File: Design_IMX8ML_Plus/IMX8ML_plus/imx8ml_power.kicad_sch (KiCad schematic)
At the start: 33 parts

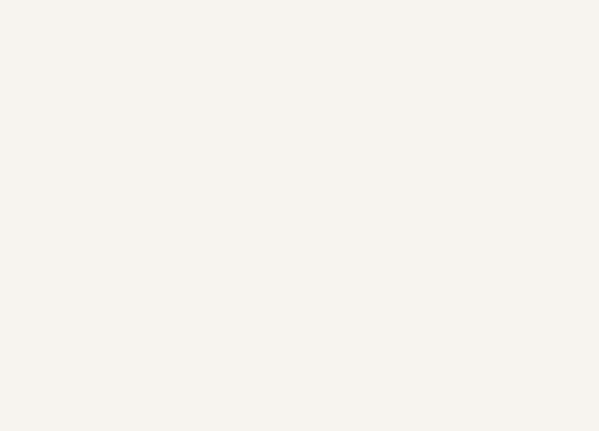
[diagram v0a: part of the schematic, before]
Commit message: Add resistors to PMIC
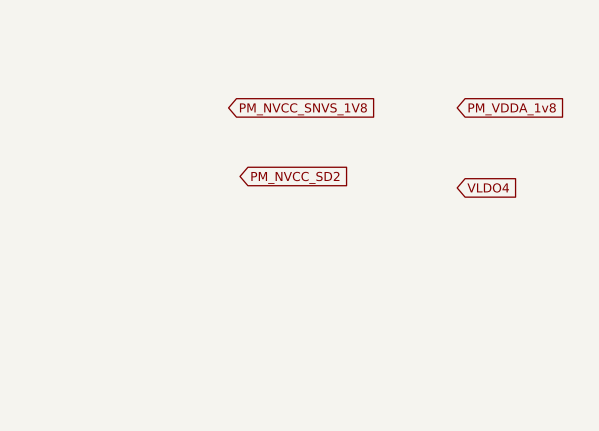
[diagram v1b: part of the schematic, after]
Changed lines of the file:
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@@
     (effects (font (size 1.27 1.27)) (justify left bottom))
+  )
+  (global_label "PM_VDDA_1v8" (shape input) (at 260.35 29.21 0) (fields_autoplaced)
+    (effects (font (size 1 1)) (justify left))
+    (property "Intersheetrefs" "${INTERSHEET_REFS}" (at 272.6855 29.21 0)
+      (effects (font (size 1.27 1.27)) (justify left) hide)
+    )
   )
   (global_label "PM_NVCC_DRAM_1V1" (shape input) (at 34.29 80.01 180) (fields_autoplaced)
@@
     )
   )
+  (global_label "PM_NVCC_SD2" (shape input) (at 236.22 36.83 0) (fields_autoplaced)
+    (effects (font (size 1 1)) (justify left))
+    (property "Intersheetrefs" "${INTERSHEET_REFS}" (at 248.9841 36.83 0)
+      (effects (font (size 1.27 1.27)) (justify left) hide)
+    )
+  )
+  (global_label "PM_NVCC_SNVS_1V8" (shape input) (at 234.95 29.21 0) (fields_autoplaced)
+    (effects (font (size 1 1)) (justify left))
+    (property "Intersheetrefs" "${INTERSHEET_REFS}" (at 252.1426 29.21 0)
+      (effects (font (size 1.27 1.27)) (justify left) hide)
+    )
+  )
+  (global_label "VLDO4" (shape input) (at 260.35 38.1 0) (fields_autoplaced)
+    (effects (font (size 1 1)) (justify left))
+    (property "Intersheetrefs" "${INTERSHEET_REFS}" (at 267.3045 38.1 0)
+      (effects (font (size 1.27 1.27)) (justify left) hide)
+    )
+  )

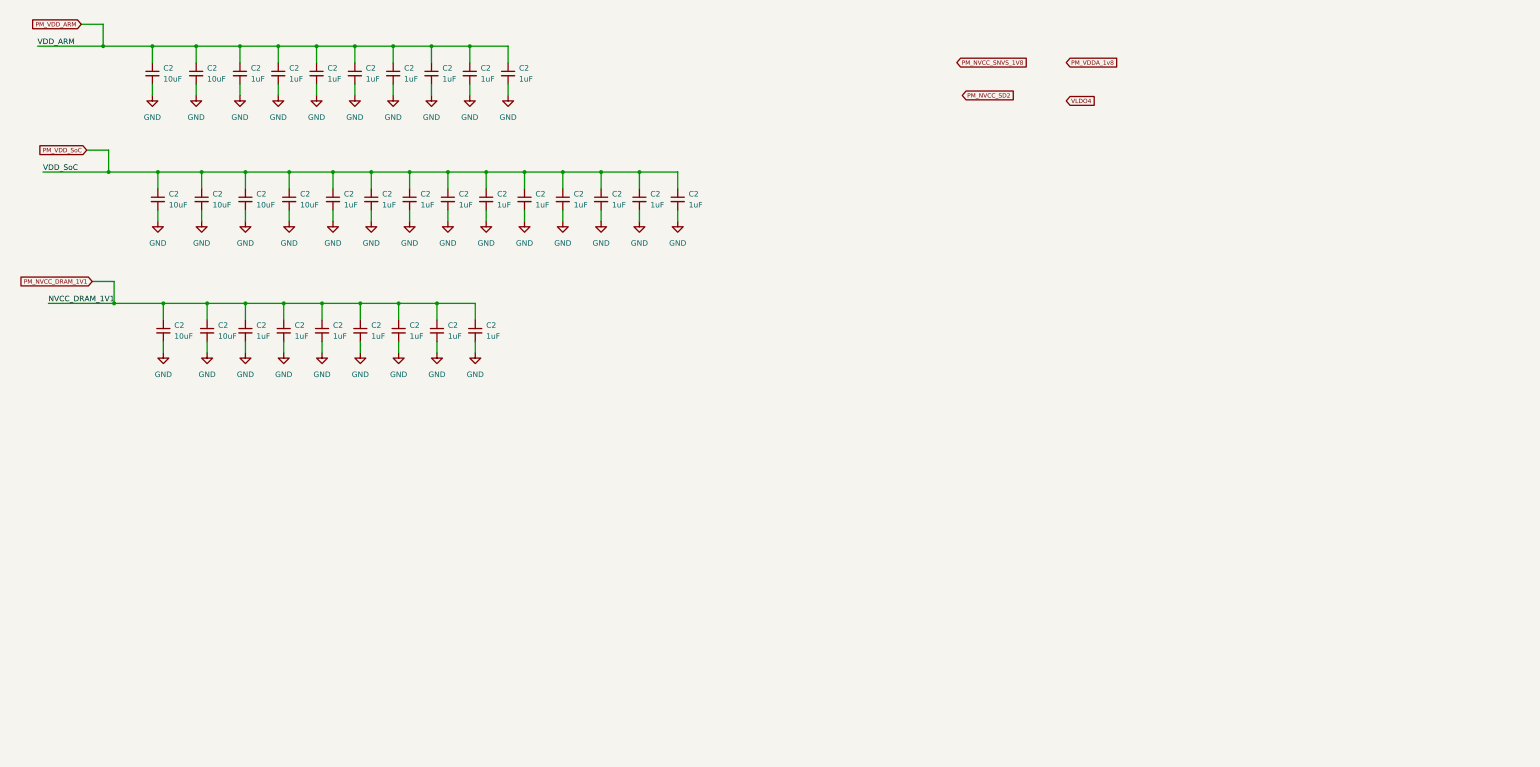
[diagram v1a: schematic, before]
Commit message: Add interface io pins
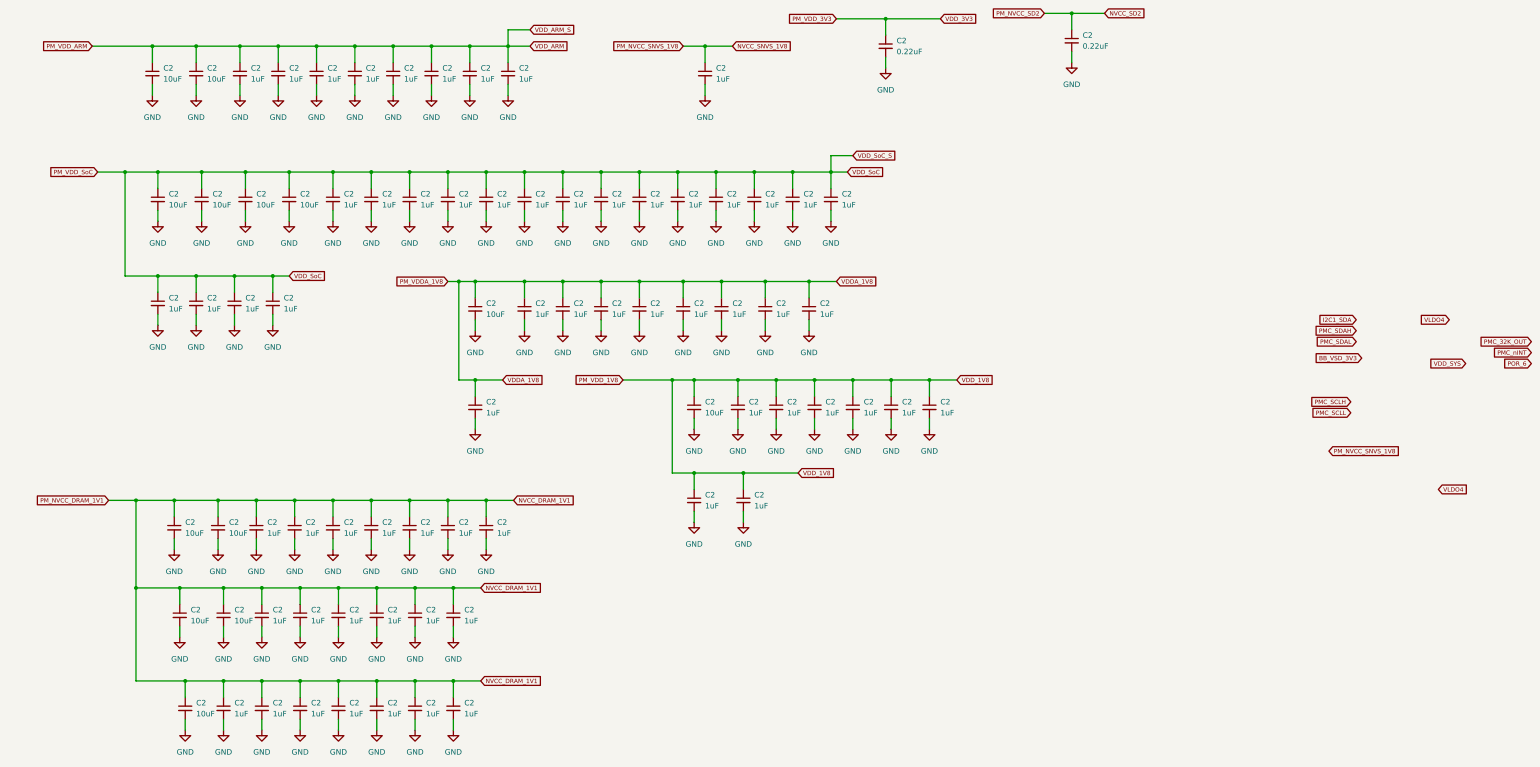
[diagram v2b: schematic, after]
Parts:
- added C2 (x39): 1uF, Capacitor_SMD:C_0201_0603Metric_Pad0.64x0.40mm_HandSolder, symbol Device:C_Small
- added C2 (x5): 10uF, Capacitor_SMD:C_0402_1005Metric, symbol Device:C_Small
- added C2 (x2): 0.22uF, Capacitor_SMD:C_0201_0603Metric_Pad0.64x0.40mm_HandSolder, symbol Device:C_Small
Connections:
- net GND: now also C2.2, C2.2, C2.2, C2.2, C2.2, C2.2, C2.2, C2.2, C2.2, C2.2, C2.2, C2.2, C2.2, C2.2, C2.2, C2.2, C2.2, C2.2, C2.2, C2.2, C2.2, C2.2, C2.2, C2.2, C2.2, C2.2, C2.2, C2.2, C2.2, C2.2, C2.2, C2.2, C2.2, C2.2, C2.2, C2.2, C2.2, C2.2, C2.2, C2.2, C2.2, C2.2, C2.2, C2.2, C2.2, C2.2
- net PM_VDD_SoC: now also C2.1, C2.1, C2.1, C2.1, C2.1, C2.1, C2.1, C2.1
- net PM_NVCC_DRAM_1V1 renamed NVCC_DRAM_1V1
- net NVCC_DRAM_1V1: now also C2.1, C2.1, C2.1, C2.1, C2.1, C2.1, C2.1, C2.1, C2.1, C2.1, C2.1, C2.1, C2.1, C2.1, C2.1, C2.1
- new net NVCC_SD2: C2.1
- new net NVCC_SNVS_1V8: C2.1
- new net PM_VDDA_1V8: C2.1, C2.1, C2.1, C2.1, C2.1, C2.1, C2.1, C2.1, C2.1, C2.1
- new net PM_VDD_1V8: C2.1, C2.1, C2.1, C2.1, C2.1, C2.1, C2.1, C2.1, C2.1
- new net PM_VDD_3V3: C2.1
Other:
- moved on the sheet: C2

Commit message: processor capacitors location
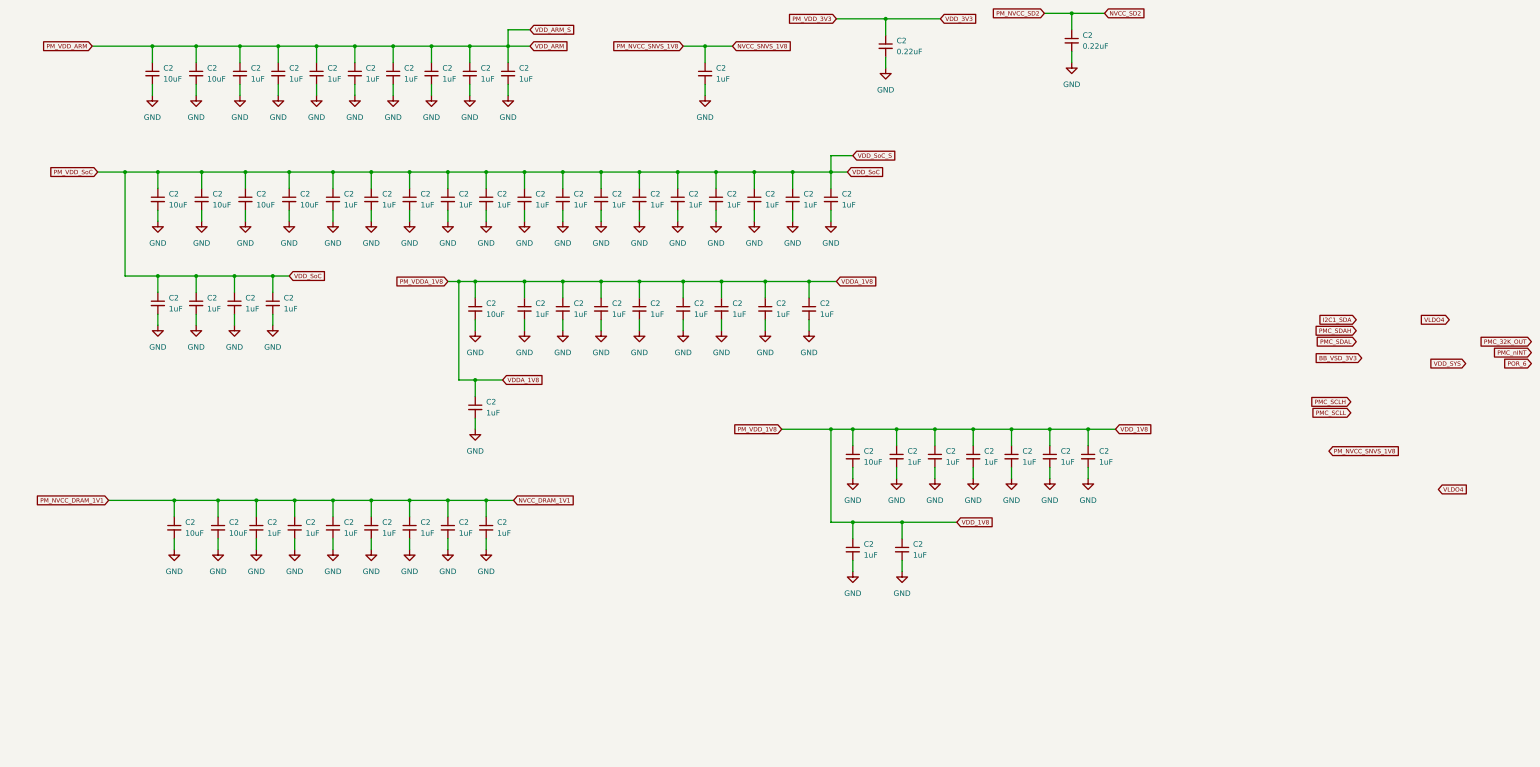
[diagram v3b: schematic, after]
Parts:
- removed C2 (x13): 1uF, Capacitor_SMD:C_0201_0603Metric_Pad0.64x0.40mm_HandSolder, symbol Device:C_Small
- removed C2 (x3): 10uF, Capacitor_SMD:C_0402_1005Metric, symbol Device:C_Small
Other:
- moved on the sheet: C2

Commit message: Add SPB228 WIFI/BLE module
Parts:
- renumbered C2 to C100, C2 to C101, C2 to C102, C2 to C103, C2 to C104, C2 to C105, C2 to C106, C2 to C107, C2 to C108, C2 to C109, C2 to C110, C2 to C111, C2 to C112, C2 to C113, C2 to C114, C2 to C115, C2 to C116, C2 to C117, C2 to C118, C2 to C119, C2 to C120, C2 to C121, C2 to C122, C2 to C123, C2 to C132, C2 to C141, C2 to C25, C2 to C26, C2 to C27, C2 to C28, C2 to C29, C2 to C30, C2 to C31, C2 to C32, C2 to C33, C2 to C34, C2 to C35, C2 to C36, C2 to C37, C2 to C38, C2 to C39, C2 to C40, C2 to C41, C2 to C42, C2 to C43, C2 to C44, C2 to C45, C2 to C46, C2 to C47, C2 to C48, C2 to C49, C2 to C50, C2 to C56, C2 to C57, C2 to C58, C2 to C59, C2 to C60, C2 to C61, C2 to C62, C2 to C96, C2 to C97, C2 to C98, C2 to C99

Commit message: reorganization of the componentes
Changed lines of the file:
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@@
 	(global_label "BB_VSD_3V3"
 		(shape input)
-		(at 328.93 97.79 180)
-		(fields_autoplaced yes)
-		(effects
-			(font
-				(size 1 1)
-			)
-			(justify right)
-		)
-		(property "Intersheetrefs" "${INTERSHEET_REFS}"
-			(at 317.5469 97.79 0)
+		(at 242.57 62.23 180)
+		(fields_autoplaced yes)
+		(effects
+			(font
+				(size 1 1)
+			)
+			(justify right)
+		)
+		(property "Intersheetrefs" "${INTERSHEET_REFS}"
+			(at 231.1869 62.23 0)
 			(effects
 				(font
@@
 	(global_label "I2C1_SDA"
 		(shape input)
-		(at 327.66 88.9 180)
-		(fields_autoplaced yes)
-		(effects
-			(font
-				(size 1 1)
-			)
-			(justify right)
-		)
-		(property "Intersheetrefs" "${INTERSHEET_REFS}"
-			(at 318.4197 88.9 0)
+		(at 241.3 53.34 180)
+		(fields_autoplaced yes)
+		(effects
+			(font
+				(size 1 1)
+			)
+			(justify right)
+		)
+		(property "Intersheetrefs" "${INTERSHEET_REFS}"
+			(at 232.0597 53.34 0)
 			(effects
 				(font
@@
 	(global_label "VLDO4"
 		(shape input)
-		(at 349.25 88.9 180)
-		(fields_autoplaced yes)
-		(effects
-			(font
-				(size 1 1)
-			)
-			(justify right)
-		)
-		(property "Intersheetrefs" "${INTERSHEET_REFS}"
-			(at 342.2955 88.9 0)
+		(at 262.89 53.34 180)
+		(fields_autoplaced yes)
+		(effects
+			(font
+				(size 1 1)
+			)
+			(justify right)
+		)
+		(property "Intersheetrefs" "${INTERSHEET_REFS}"
+			(at 255.9355 53.34 0)
 			(effects
 				(font
@@
 	(global_label "PMC_SCLH"
 		(shape input)
-		(at 326.39 107.95 180)
-		(fields_autoplaced yes)
-		(effects
-			(font
-				(size 1 1)
-			)
-			(justify right)
-		)
-		(property "Intersheetrefs" "${INTERSHEET_REFS}"
-			(at 316.3878 107.95 0)
+		(at 240.03 72.39 180)
+		(fields_autoplaced yes)
+		(effects
+			(font
+				(size 1 1)
+			)
+			(justify right)
+		)
+		(property "Intersheetrefs" "${INTERSHEET_REFS}"
+			(at 230.0278 72.39 0)
 			(effects
 				(font
@@
 	(global_label "PMC_SCLL"
 		(shape input)
-		(at 326.39 110.49 180)
-		(fields_autoplaced yes)
-		(effects
-			(font
-				(size 1 1)
-			)
-			(justify right)
-		)
-		(property "Intersheetrefs" "${INTERSHEET_REFS}"
-			(at 316.6259 110.49 0)
+		(at 240.03 74.93 180)
+		(fields_autoplaced yes)
+		(effects
+			(font
+				(size 1 1)
+			)
+			(justify right)
+		)
+		(property "Intersheetrefs" "${INTERSHEET_REFS}"
+			(at 230.2659 74.93 0)
 			(effects
 				(font
@@
 	(global_label "PMC_SDAH"
 		(shape input)
-		(at 327.66 91.44 180)
-		(fields_autoplaced yes)
-		(effects
-			(font
-				(size 1 1)
-			)
-			(justify right)
-		)
-		(property "Intersheetrefs" "${INTERSHEET_REFS}"
-			(at 317.6102 91.44 0)
+		(at 241.3 55.88 180)
+		(fields_autoplaced yes)
+		(effects
+			(font
+				(size 1 1)
+			)
+			(justify right)
+		)
+		(property "Intersheetrefs" "${INTERSHEET_REFS}"
+			(at 231.2502 55.88 0)
 			(effects
 				(font
@@
 	(global_label "POR_6"
 		(shape input)
-		(at 368.3 99.06 180)
-		(fields_autoplaced yes)
-		(effects
-			(font
-				(size 1 1)
-			)
-			(justify right)
-		)
-		(property "Intersheetrefs" "${INTERSHEET_REFS}"
-			(at 361.2502 99.06 0)
+		(at 281.94 63.5 180)
+		(fields_autoplaced yes)
+		(effects
+			(font
+				(size 1 1)
+			)
+			(justify right)
+		)
+		(property "Intersheetrefs" "${INTERSHEET_REFS}"
+			(at 274.8902 63.5 0)
 			(effects
 				(font
@@
 	(global_label "PMC_32K_OUT"
 		(shape input)
-		(at 368.3 93.98 180)
-		(fields_autoplaced yes)
-		(effects
-			(font
-				(size 1 1)
-			)
-			(justify right)
-		)
-		(property "Intersheetrefs" "${INTERSHEET_REFS}"
-			(at 355.5835 93.98 0)
+		(at 281.94 58.42 180)
+		(fields_autoplaced yes)
+		(effects
+			(font
+				(size 1 1)
+			)
+			(justify right)
+		)
+		(property "Intersheetrefs" "${INTERSHEET_REFS}"
+			(at 269.2235 58.42 0)
 			(effects
 				(font
@@
 	(global_label "PMC_SDAL"
 		(shape input)
-		(at 327.66 93.98 180)
-		(fields_autoplaced yes)
-		(effects
-			(font
-				(size 1 1)
-			)
-			(justify right)
-		)
-		(property "Intersheetrefs" "${INTERSHEET_REFS}"
-			(at 317.8483 93.98 0)
+		(at 241.3 58.42 180)
+		(fields_autoplaced yes)
+		(effects
+			(font
+				(size 1 1)
+			)
+			(justify right)
+		)
+		(property "Intersheetrefs" "${INTERSHEET_REFS}"
+			(at 231.4883 58.42 0)
 			(effects
 				(font
@@
 	(global_label "PMC_nINT"
 		(shape input)
-		(at 368.3 96.52 180)
-		(fields_autoplaced yes)
-		(effects
-			(font
-				(size 1 1)
-			)
-			(justify right)
-		)
-		(property "Intersheetrefs" "${INTERSHEET_REFS}"
-			(at 358.9168 96.52 0)
+		(at 281.94 60.96 180)
+		(fields_autoplaced yes)
+		(effects
+			(font
+				(size 1 1)
+			)
+			(justify right)
+		)
+		(property "Intersheetrefs" "${INTERSHEET_REFS}"
+			(at 272.5568 60.96 0)
 			(effects
 				(font
@@
 	(global_label "PM_NVCC_SNVS_1V8"
 		(shape input)
-		(at 321.31 119.38 0)
-		(fields_autoplaced yes)
-		(effects
-			(font
-				(size 1 1)
-			)
-			(justify left)
-		)
-		(property "Intersheetrefs" "${INTERSHEET_REFS}"
-			(at 338.5026 119.38 0)
+		(at 234.95 83.82 0)
+		(fields_autoplaced yes)
+		(effects
+			(font
+				(size 1 1)
+			)
+			(justify left)
+		)
+		(property "Intersheetrefs" "${INTERSHEET_REFS}"
+			(at 252.1426 83.82 0)
 			(effects
 				(font
@@
 	(global_label "VDD_SYS"
 		(shape input)
-		(at 353.06 99.06 180)
-		(fields_autoplaced yes)
-		(effects
-			(font
-				(size 1 1)
-			)
-			(justify right)
-		)
-		(property "Intersheetrefs" "${INTERSHEET_REFS}"
-			(at 344.3912 99.06 0)
+		(at 266.7 63.5 180)
+		(fields_autoplaced yes)
+		(effects
+			(font
+				(size 1 1)
+			)
+			(justify right)
+		)
+		(property "Intersheetrefs" "${INTERSHEET_REFS}"
+			(at 258.0312 63.5 0)
 			(effects
 				(font
@@
 	(global_label "VLDO4"
 		(shape input)
-		(at 346.71 128.27 0)
-		(fields_autoplaced yes)
-		(effects
-			(font
-				(size 1 1)
-			)
-			(justify left)
-		)
-		(property "Intersheetrefs" "${INTERSHEET_REFS}"
-			(at 353.6645 128.27 0)
-			(effects
-				(font
+		(at 260.35 92.71 0)
+		(fields_autoplaced yes)
+		(effects
+			(font
+				(size 1 1)
+			)
+			(justify left)
+		)
+		(property "Intersheetrefs" "${INTERSHEET_REFS}"
+			(at 267.3045 92.71 0)
+			(effects
+				(font

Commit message: [PROCESSOR] Create zones It added power zones in the four layer
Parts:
- renumbered C112 to C100, C99 to C101, C113 to C102, C100 to C103, C116 to C104, C123 to C105, C132 to C106, C117 to C107, C115 to C108, C118 to C109, C119 to C110, C120 to C111, C121 to C112, C141 to C113, C122 to C114, C25 to C52, C35 to C53, C101 to C54, C49 to C55, C26 to C56, C102 to C57, C36 to C58, C50 to C59, C103 to C60, C27 to C61, C45 to C62, C56 to C63, C104 to C64, C28 to C65, C46 to C66, C57 to C67, C29 to C68, C37 to C69, C58 to C70, C30 to C71, C38 to C72, C59 to C73, C31 to C74, C39 to C75, C60 to C76, C32 to C77, C40 to C78, C61 to C79, C33 to C80, C111 to C81, C114 to C82, C41 to C83, C62 to C84, C34 to C85, C42 to C86, C105 to C87, C43 to C88, C106 to C89, C44 to C90, C107 to C91, C47 to C92, C108 to C93, C48 to C94, C109 to C95, C110 to C98, C98 to C99

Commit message: [BB_IMX8MLP IMX8MLP] Actuallizated to 9.0 kicad version
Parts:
- C100, C101, C102, C103, C105, C107, C108, C109, C110, C111, C112, C114, C54, C57, C60, C61, C63, C64, C65, C67, C68, C69, C70, C71, C72, C73, C74, C75, C76, C77, C78, C79, C80, C82, C83, C84, C85, C86, C87, C88, C89, C90, C91, C92, C93, C94, C95, C96, C97, C98, C99: footprint Capacitor_SMD:C_0201_0603Metric_Pad0.64x0.40mm_HandSolder -> Capacitor_SMD:C_0201_0603Metric; MP (none) -> 02016D105MAT2A; Price (none) -> 0.1
- C104, C52, C53, C55, C56, C58, C59, C62, C66, C81: MP (none) -> CL05A106MQ5NUNC; Price (none) -> 0.1
- C106, C113: footprint Capacitor_SMD:C_0201_0603Metric_Pad0.64x0.40mm_HandSolder -> Capacitor_SMD:C_0201_0603Metric; MP (none) -> LMK063BJ224MP-F; Price (none) -> 0.11

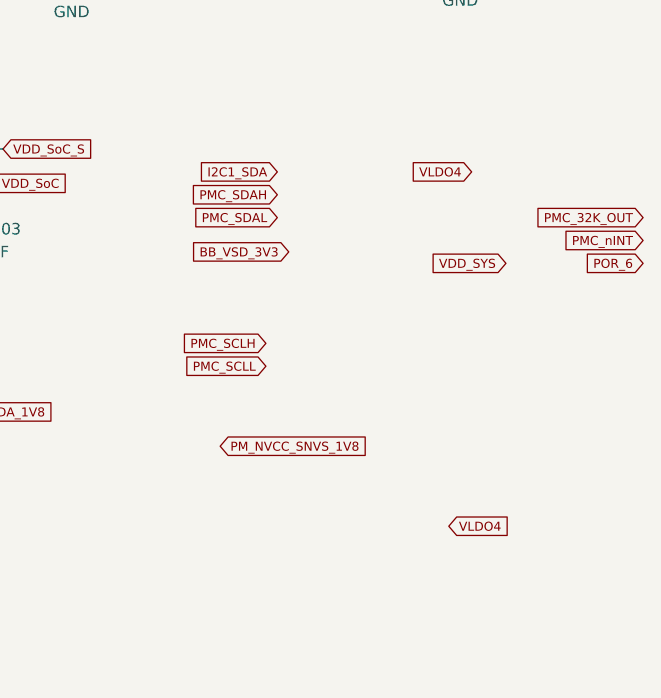
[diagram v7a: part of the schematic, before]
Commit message: [IMX8ML] Add new layer
A new layers was add in the cpu schematic, now it had 8 layer.
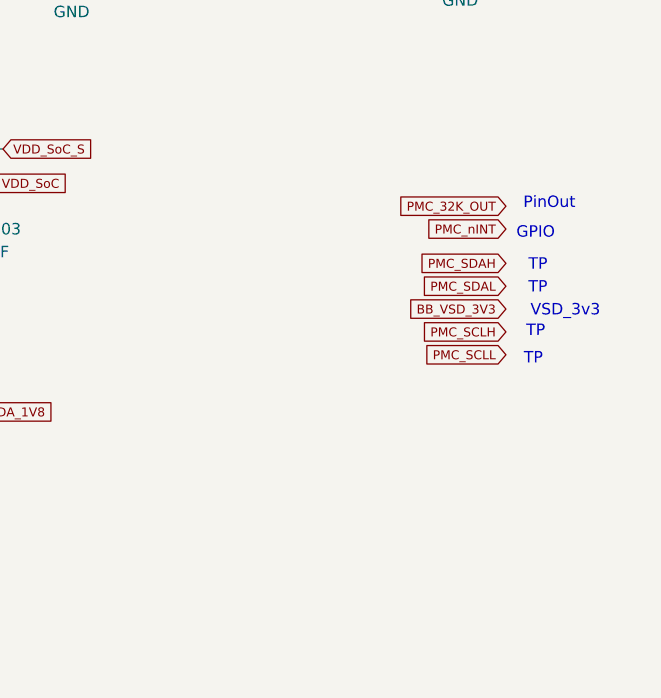
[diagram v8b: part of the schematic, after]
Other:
- note added: "GPIO"
- note added: "PinOut"
- note added: "TP"
- note added: "VSD_3v3"
